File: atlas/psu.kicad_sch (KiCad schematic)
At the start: 45 parts, among them Q201 2N7002, Q202 IRLR3636, Q203 IRLR3636, U201 TLS115D0EJ, U202 TLS115D0EJ, U203 TLS115D0EJ, U204 TPS70933DBV, U205 LMR14020

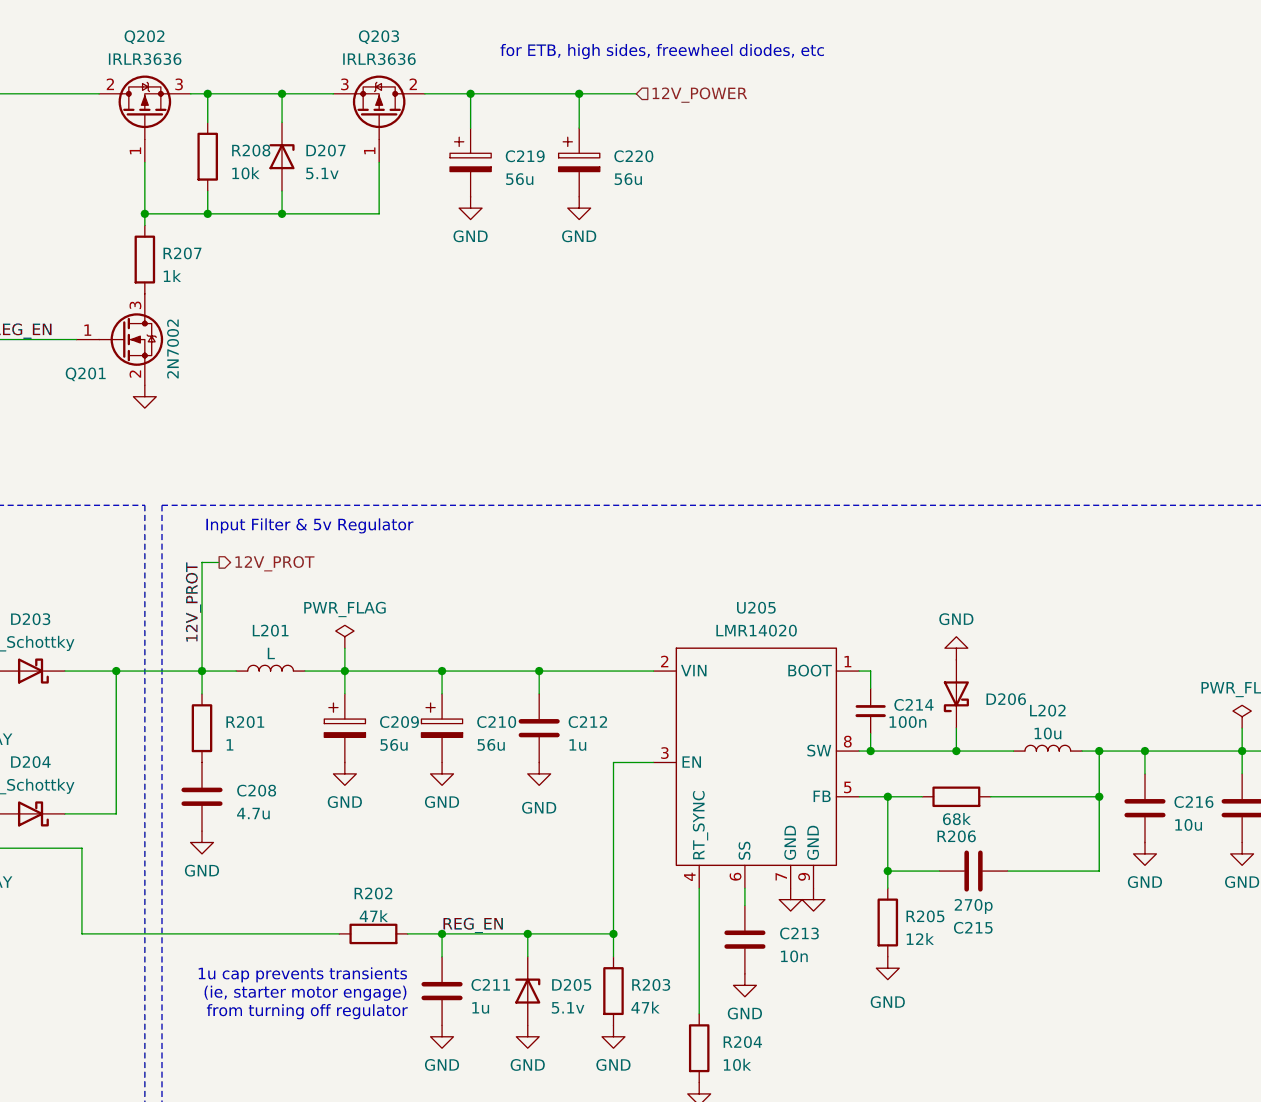
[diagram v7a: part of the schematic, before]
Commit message: footprints & lcsc
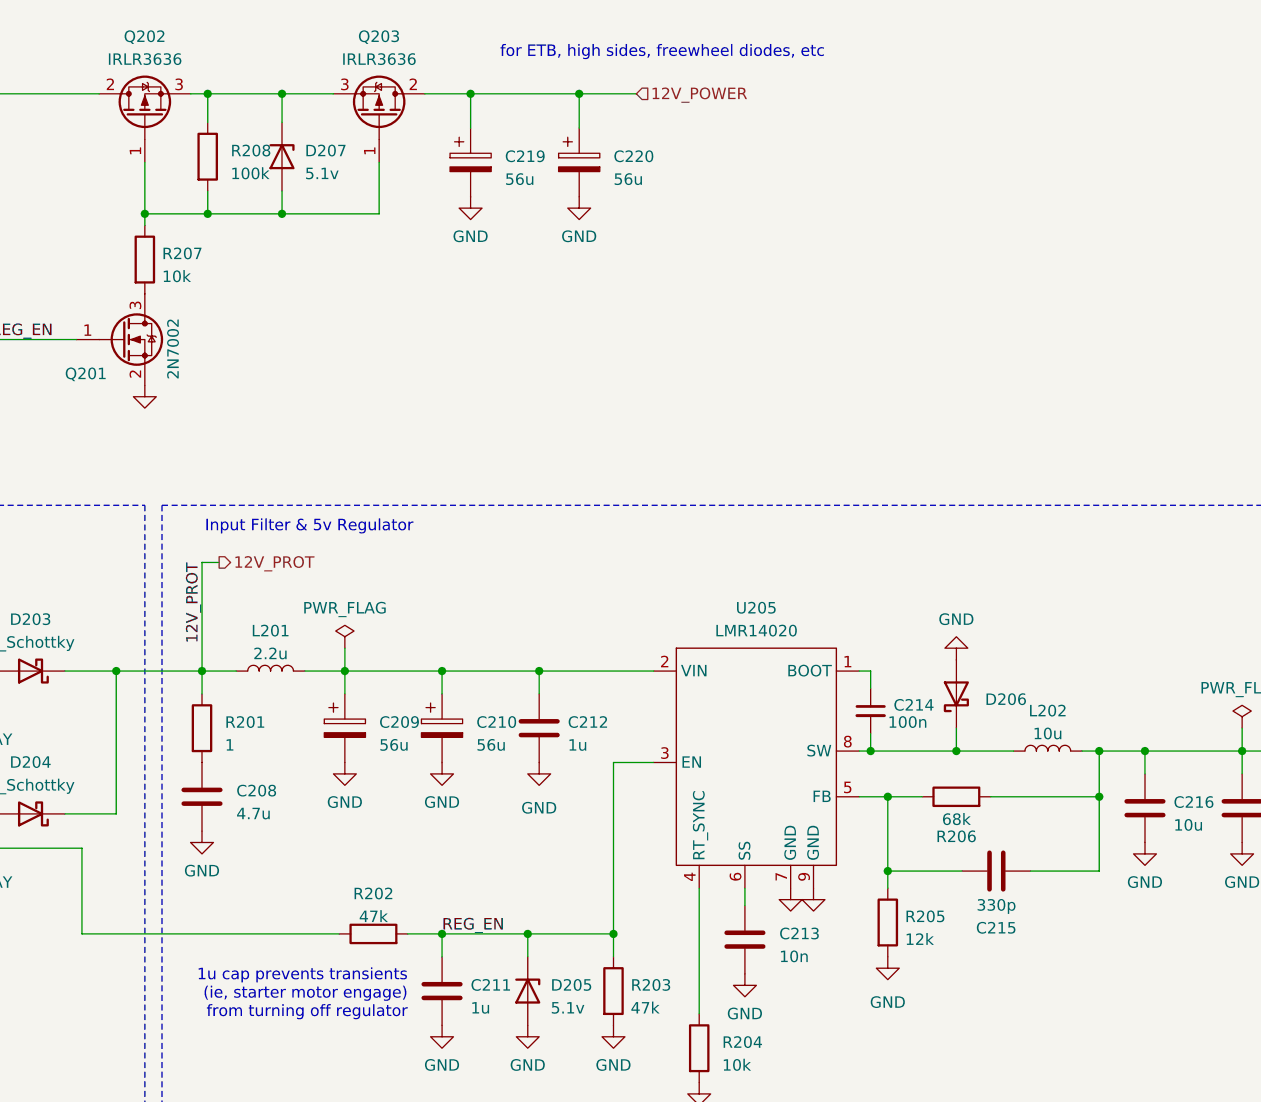
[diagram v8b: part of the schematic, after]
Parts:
- C215: value 270p -> 330p; footprint (none) -> Capacitor_SMD:C_0402_1005Metric; LCSC (none) -> C13533
- L201: value L -> 2.2u; footprint (none) -> Inductor_SMD:L_Wuerth_MAPI-3015; LCSC (none) -> C167747
- L202: footprint (none) -> sunlort-MWSA0503:MWSA0503; LCSC (none) -> C408412
- R207: value 1k -> 10k; footprint (none) -> Resistor_SMD:R_0402_1005Metric; LCSC (none) -> C25744
- R208: value 10k -> 100k; footprint (none) -> Resistor_SMD:R_0402_1005Metric; LCSC (none) -> C25741
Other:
- moved on the sheet: C215
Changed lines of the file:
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@@
     (stroke (width 0) (type solid) (color 0 0 0 0))
   )
-  (wire (pts (xy 167.005 138.43) (xy 172.72 138.43))
+  (wire (pts (xy 167.005 138.43) (xy 175.26 138.43))
     (stroke (width 0) (type solid) (color 0 0 0 0))
   )
@@
     (stroke (width 0) (type solid) (color 0 0 0 0))
   )
-  (wire (pts (xy 180.34 138.43) (xy 190.5 138.43))
+  (wire (pts (xy 182.88 138.43) (xy 190.5 138.43))
     (stroke (width 0) (type solid) (color 0 0 0 0))
   )
@@
     (in_bom yes) (on_board yes) (fields_autoplaced)
     (property "Reference" "L201" (id 0) (at 98.425 111.76 90))
-    (property "Value" "L" (id 1) (at 98.425 114.3 90))
-    (property "Footprint" "" (id 2) (at 98.425 116.205 0)
+    (property "Value" "2.2u" (id 1) (at 98.425 114.3 90))
+    (property "Footprint" "Inductor_SMD:L_Wuerth_MAPI-3015" (id 2) (at 98.425 116.205 0)
       (effects (font (size 1.27 1.27)) hide)
     )
     (property "Datasheet" "~" (id 3) (at 98.425 116.205 0)
+      (effects (font (size 1.27 1.27)) hide)
+    )
+    (property "LCSC" "C167747" (id 4) (at 98.425 116.205 0)
       (effects (font (size 1.27 1.27)) hide)
     )
@@
     (property "Reference" "L202" (id 0) (at 184.785 120.65 90))
     (property "Value" "10u" (id 1) (at 184.785 123.19 90))
-    (property "Footprint" "" (id 2) (at 184.785 125.095 0)
+    (property "Footprint" "sunlort-MWSA0503:MWSA0503" (id 2) (at 184.785 125.095 0)
       (effects (font (size 1.27 1.27)) hide)
     )
@@
       (effects (font (size 1.27 1.27)) hide)
     )
+    (property "LCSC" "C408412" (id 4) (at 184.785 125.095 0)
+      (effects (font (size 1.27 1.27)) hide)
+    )
     (pin "1")
     (pin "2")
@@
       (effects (font (size 1.27 1.27)) (justify left))
     )
-    (property "Value" "1k" (id 1) (at 86.36 72.3899 0)
-      (effects (font (size 1.27 1.27)) (justify left))
-    )
-    (property "Footprint" "" (id 2) (at 82.677 70.485 90)
+    (property "Value" "10k" (id 1) (at 86.36 72.3899 0)
+      (effects (font (size 1.27 1.27)) (justify left))
+    )
+    (property "Footprint" "Resistor_SMD:R_0402_1005Metric" (id 2) (at 82.677 70.485 90)
       (effects (font (size 1.27 1.27)) hide)
     )
@@
       (effects (font (size 1.27 1.27)) hide)
     )
+    (property "LCSC" "C25744" (id 4) (at 84.455 70.485 0)
+      (effects (font (size 1.27 1.27)) hide)
+    )
     (pin "1")
     (pin "2")
@@
       (effects (font (size 1.27 1.27)) (justify left))
     )
-    (property "Value" "10k" (id 1) (at 93.98 60.9599 0)
-      (effects (font (size 1.27 1.27)) (justify left))
-    )
-    (property "Footprint" "" (id 2) (at 89.662 59.055 90)
+    (property "Value" "100k" (id 1) (at 93.98 60.9599 0)
+      (effects (font (size 1.27 1.27)) (justify left))
+    )
+    (property "Footprint" "Resistor_SMD:R_0402_1005Metric" (id 2) (at 89.662 59.055 90)
       (effects (font (size 1.27 1.27)) hide)
     )
     (property "Datasheet" "~" (id 3) (at 91.44 59.055 0)
+      (effects (font (size 1.27 1.27)) hide)
+    )
+    (property "LCSC" "C25741" (id 4) (at 91.44 59.055 0)
       (effects (font (size 1.27 1.27)) hide)
     )
@@
     (pin "2")
   )
-  (symbol (lib_id "Device:C") (at 176.53 138.43 270) (unit 1)
+  (symbol (lib_id "Device:C") (at 179.07 138.43 270) (unit 1)
     (in_bom yes) (on_board yes)
-    (property "Reference" "C215" (id 0) (at 176.53 144.78 90))
-    (property "Value" "270p" (id 1) (at 176.53 142.24 90))
-    (property "Footprint" "" (id 2) (at 172.72 139.3952 0)
-      (effects (font (size 1.27 1.27)) hide)
-    )
-    (property "Datasheet" "~" (id 3) (at 176.53 138.43 0)
-      (effects (font (size 1.27 1.27)) hide)
-    )
+    (property "Reference" "C215" (id 0) (at 179.07 144.78 90))
+    (property "Value" "330p" (id 1) (at 179.07 142.24 90))
+    (property "Footprint" "Capacitor_SMD:C_0402_1005Metric" (id 2) (at 175.26 139.3952 0)
+      (effects (font (size 1.27 1.27)) hide)
+    )
+    (property "Datasheet" "~" (id 3) (at 179.07 138.43 0)
+      (effects (font (size 1.27 1.27)) hide)
+    )
+    (property "LCSC" "C13533" (id 4) (at 179.07 138.43 0)
+      (effects (font (size 1.27 1.27)) hide)
+    )
